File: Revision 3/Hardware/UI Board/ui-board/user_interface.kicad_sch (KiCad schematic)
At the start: 0 parts

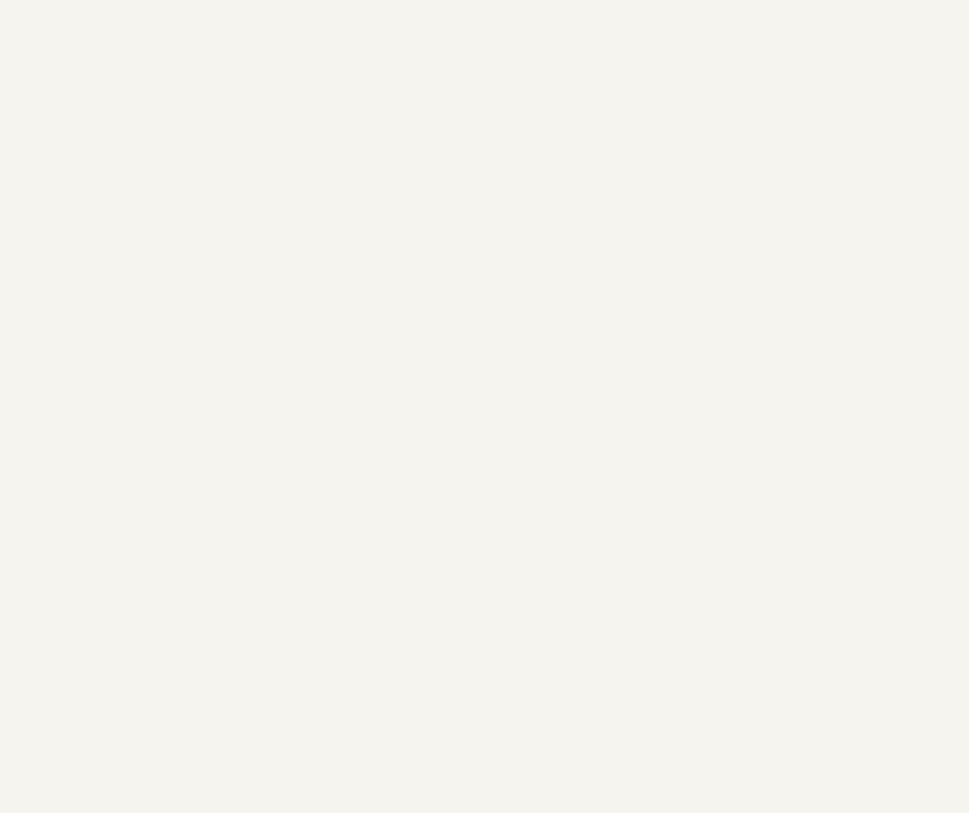
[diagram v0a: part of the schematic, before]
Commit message: Add keypad to schematic
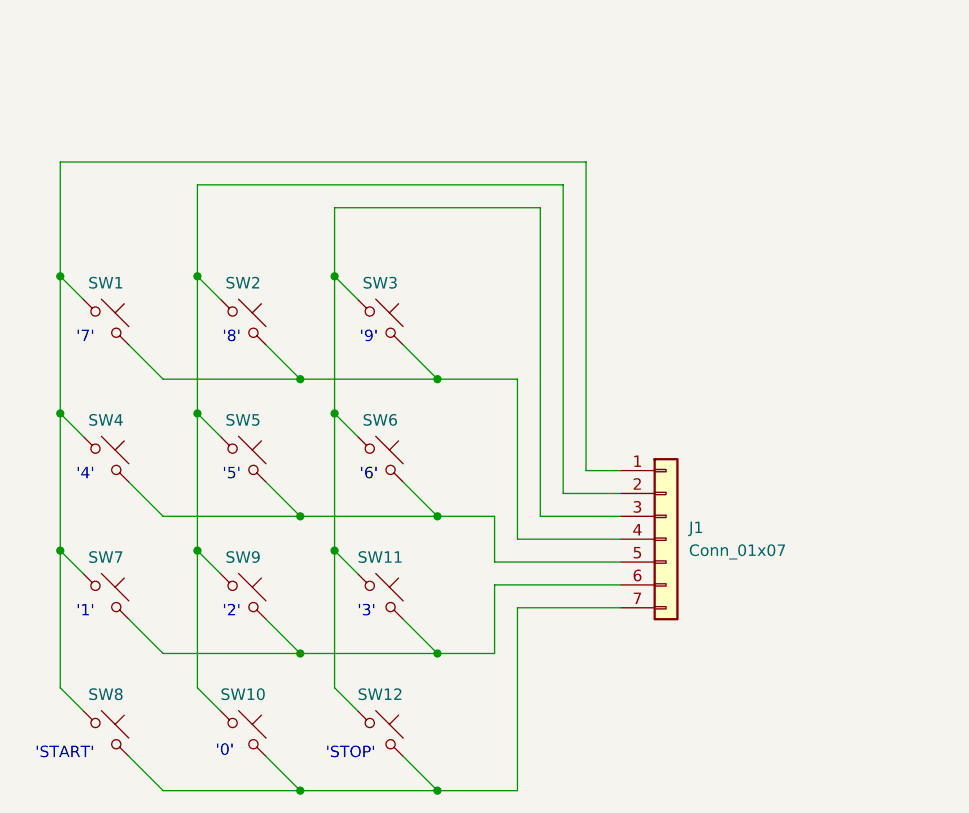
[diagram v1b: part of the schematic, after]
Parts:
- added J1: Conn_01x07, Connector_PinHeader_2.54mm:PinHeader_1x07_P2.54mm_Vertical, symbol Connector_Generic:Conn_01x07
- added SW1, SW10, SW11, SW12, SW2, SW3, SW4, SW5, SW6, SW7, SW8, SW9: SW_Push_45deg, Button_Switch_Keyboard:SW_Cherry_MX_1.00u_PCB, symbol Switch:SW_Push_45deg
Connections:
- new net: J1.1 (Pin_1), SW1.1, SW4.1, SW7.1, SW8.1
- new net: J1.6 (Pin_6), SW11.2, SW7.2, SW9.2
- new net: J1.3 (Pin_3), SW11.1, SW12.1, SW3.1, SW6.1
- new net: J1.7 (Pin_7), SW10.2, SW12.2, SW8.2
- new net: J1.5 (Pin_5), SW4.2, SW5.2, SW6.2
- new net: J1.2 (Pin_2), SW10.1, SW2.1, SW5.1, SW9.1
- new net: J1.4 (Pin_4), SW1.2, SW2.2, SW3.2
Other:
- note added: "'0'"
- note added: "'1'"
- note added: "'2'"
- note added: "'3'"
- note added: "'4'"
- note added: "'5'"
- note added: "'6'"
- note added: "'7'"
- note added: "'8'"
- note added: "'9'"
- note added: "'START'"
- note added: "'STOP'"

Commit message: board complete and fab files generated, sent to fab
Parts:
- removed J1: Conn_01x07, Connector_PinHeader_2.54mm:PinHeader_1x07_P2.54mm_Vertical, symbol Connector_Generic:Conn_01x07
- added BZ1: PT-1306T, Buzzer_Beeper:Buzzer_12x9.5RM7.6, symbol Device:Buzzer
- added H1, H2, H3, H4: MountingHole, MountingHole:MountingHole_3.2mm_M3, symbol Mechanical:MountingHole
- added H5, H6, H7, H8: MountingHole, MountingHole:MountingHole_2.2mm_M2, symbol Mechanical:MountingHole
- added J2: Conn_01x07, Connector_PinSocket_2.54mm:PinSocket_1x07_P2.54mm_Vertical, symbol Connector_Generic:Conn_01x07
- added J3: Conn_01x07, Connector_PinHeader_2.54mm:PinHeader_1x07_P2.54mm_Vertical, symbol Connector_Generic:Conn_01x07
- added J4: Conn_01x09, Connector_PinHeader_2.54mm:PinHeader_1x09_P2.54mm_Vertical, symbol Connector_Generic:Conn_01x09
- added R1: 1k, Resistor_SMD:R_0603_1608Metric_Pad0.98x0.95mm_HandSolder, symbol Device:R_US
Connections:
- net Col_0: now reaches SW1.1, SW4.1, SW7.1, SW8.1
- net Col_0: now also J4.3 (Pin_3)
- net Row_2: now reaches SW11.2, SW7.2, SW9.2
- net Row_2: now also J4.6 (Pin_6)
- net Col_2: now reaches SW11.1, SW12.1, SW3.1, SW6.1
- net Col_2: now also J4.1 (Pin_1)
- net Row_3: now reaches SW10.2, SW12.2, SW8.2
- net Row_3: now also J4.7 (Pin_7)
- net Row_1: now reaches SW4.2, SW5.2, SW6.2
- net Row_1: now also J4.5 (Pin_5)
- net Col_1: now reaches SW10.1, SW2.1, SW5.1, SW9.1
- net Col_1: now also J4.2 (Pin_2)
- net Row_0: now reaches SW1.2, SW2.2, SW3.2
- net Row_0: now also J4.4 (Pin_4)
- new net: BZ1.1 (+), J4.8 (Pin_8)
- new net: J4.9 (Pin_9), R1.2
- new net: BZ1.2 (-), R1.1
- new net LCD_CS: J2.7 (Pin_7), J3.7 (Pin_7)
- new net LCD_DC: J2.6 (Pin_6), J3.6 (Pin_6)
- new net LCD_GND: J2.1 (Pin_1), J3.1 (Pin_1)
- new net LCD_RES: J2.5 (Pin_5), J3.5 (Pin_5)
- new net LCD_SCK: J2.3 (Pin_3), J3.3 (Pin_3)
- new net LCD_SDA: J2.4 (Pin_4), J3.4 (Pin_4)
- new net LCD_VCC: J2.2 (Pin_2), J3.2 (Pin_2)
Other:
- note added: "Board Mounting"
- note added: "LCD Mounting"
- moved on the sheet: SW1, SW10, SW11, SW12, SW2, SW3, SW4, SW5, SW6, SW7, SW8, SW9

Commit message: regenerated fab files and sent to fab
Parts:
- R1: footprint Resistor_SMD:R_0603_1608Metric_Pad0.98x0.95mm_HandSolder -> Resistor_THT:R_Axial_DIN0204_L3.6mm_D1.6mm_P5.08mm_Horizontal
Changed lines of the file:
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@@
 			)
 		)
-		(property "Footprint" "Resistor_SMD:R_0603_1608Metric_Pad0.98x0.95mm_HandSolder"
+		(property "Footprint" "Resistor_THT:R_Axial_DIN0204_L3.6mm_D1.6mm_P5.08mm_Horizontal"
 			(at 249.174 141.986 90)
 			(effects
